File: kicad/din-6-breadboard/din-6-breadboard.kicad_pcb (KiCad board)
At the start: 2 copper layers, 41.1 x 19 mm, 21 parts, among them J1 Conn_01x03, J2 Conn_01x03, J3 Conn_01x02, J4 IN, Q1 FDC6301N, Q2 FDC6301N, Q3 FDC6301N

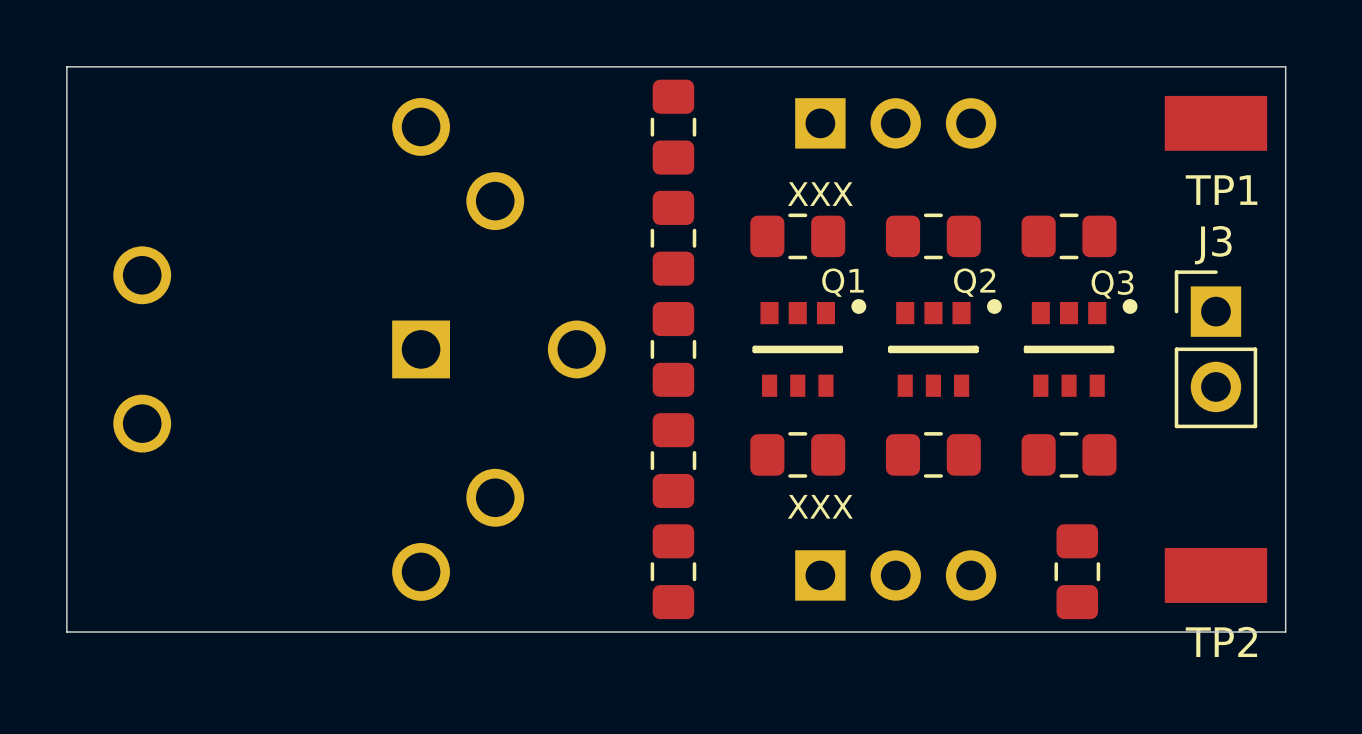
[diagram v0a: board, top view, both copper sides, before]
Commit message: pre-flood 3v and 5v
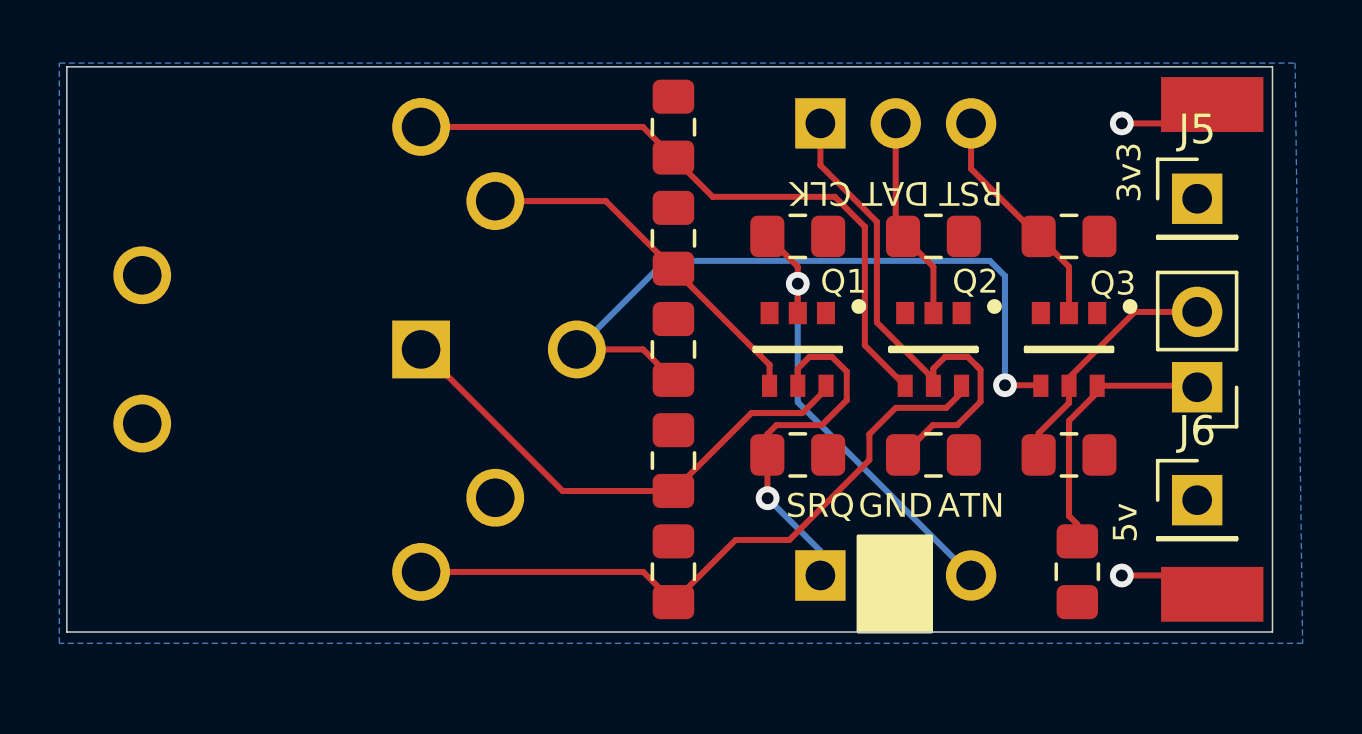
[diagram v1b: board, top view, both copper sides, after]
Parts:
- added J5: 3v3, Connector_PinHeader_2.54mm:PinHeader_1x01_P2.54mm_Vertical, F.Cu at (165.1, 124.5)
- added J6: 5v, Connector_PinHeader_2.54mm:PinHeader_1x01_P2.54mm_Vertical, F.Cu at (165.1, 134.6)
- moved R10 7.49 mm to (147.4, 129.5)
- moved R6 7.49 mm to (147.4, 137.0)
- moved J3 2.63 mm to (165.1, 130.8), turned to 180 degrees
- moved TP1 0.65 mm to (165.6, 121.3)
- moved TP2 0.65 mm to (165.6, 137.8)
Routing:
- net /RESET5: track 0.00 -> 24.6 mm, vias 0 -> 1
- net /CLK5: track 0.00 -> 22.3 mm
- net /DATA5: track 0.00 -> 22.3 mm
- net /CLK3: track 0.00 -> 17.5 mm
- net /SRQ5: track 0.00 -> 17.2 mm
- net /ATN3: track 0.00 -> 15.3 mm, vias 0 -> 1
- net /ATN5: track 0.00 -> 12.2 mm
- net /SRQ3: track 0.00 -> 12.2 mm, vias 0 -> 1
- net /Spare_Aux_H: track 0.00 -> 9.78 mm
- net /Spare_Aux_L: track 0.00 -> 9.02 mm
- net /RESET3: track 0.00 -> 7.76 mm
- net /DATA3: track 0.00 -> 6.92 mm
- net GND: track 0.00 -> 6.35 mm, vias 0 -> 2
- added copper zone on B.Cu, net GND
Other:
- board size 41.1 x 19 mm -> 40.6 x 19 mm
- net class Default: clearance 0.2 -> 0.2032; trace_width 0.25 -> 0.2032
- rule trace_clearance: 0.2 -> 0.2032
- board text added: "3v3"
- board text added: "5v"
- board text added: "ATN"
- board text added: "CLK"
- board text added: "DAT"
- board text added: "GND"
- board text added: "RST"
- board text added: "SRQ"
- board text removed: "XXX"

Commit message: breakout r1 ready for fab
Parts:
- added REF**: OSHW-Logo2_7.3x6mm_SilkScreen, Symbol:OSHW-Logo2_7.3x6mm_SilkScreen, B.Cu at (134.1, 133.6)
- added svg2mod: G***, My Libraries:BE5v2, B.Cu at (136.7, 122.9)
- J5, J6: moved to B.Cu
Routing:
- net +3V3: track 0.00 -> 21.7 mm, vias 0 -> 5
- net +5V: track 0.00 -> 4.70 mm, vias 0 -> 2
- net /CLK5: track 22.3 -> 25.3 mm
- net /Spare_Aux_H: track 9.78 -> 11.1 mm
- net /SRQ3: track 12.2 -> 12.9 mm, vias 1 -> 0
- added copper zone on F.Cu, net +3V3
- added copper zone on F.Cu, net +5V
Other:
- outline, holes or cut-outs redrawn
- board text added: "DATA"
- board text added: "Hi Chat! Thx 4 ur helpz!"
- board text added: "IEC Breakout rev1 @baldengineer"
